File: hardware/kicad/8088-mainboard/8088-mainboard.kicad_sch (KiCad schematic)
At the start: 0 parts

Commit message: Add PSB board design
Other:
- sheet EXPANSION_CONNECTOR ports: added none; removed IO_EXP2_CS, MEM_EXP2_CS
- sheet IO_DECODER ports: added none; removed IO_EXP2_CS
- sheet MEM_DECODER ports: added none; removed MEM_EXP2_CS
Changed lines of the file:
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@@
 	(wire
 		(pts
-			(xy 215.265 77.47) (xy 215.265 43.18)
-		)
-		(stroke
-			(width 0)
-			(type default)
-		)
-	)
-	(wire
-		(pts
 			(xy 108.585 96.52) (xy 113.665 96.52)
 		)
@@
 	(wire
 		(pts
-			(xy 160.655 43.18) (xy 215.265 43.18)
-		)
-		(stroke
-			(width 0)
-			(type default)
-		)
-	)
-	(wire
-		(pts
 			(xy 79.375 107.95) (xy 73.025 107.95)
 		)
@@
 	(wire
 		(pts
-			(xy 207.645 77.47) (xy 207.645 55.88)
-		)
-		(stroke
-			(width 0)
-			(type default)
-		)
-	)
-	(wire
-		(pts
 			(xy 212.725 50.8) (xy 212.725 77.47)
 		)
@@
 	(wire
 		(pts
-			(xy 207.645 55.88) (xy 126.365 55.88)
-		)
-		(stroke
-			(width 0)
-			(type default)
-		)
-	)
-	(wire
-		(pts
 			(xy 217.805 77.47) (xy 217.805 40.64)
 		)
@@
 			)
 		)
-		(pin "MEM_EXP2_CS" input
-			(at 126.365 55.88 0)
-			(effects
-				(font
-					(size 1.27 1.27)
-				)
-				(justify right)
-			)
-		)
 		(instances
 			(project "8088-mainboard"
@@
 			)
 		)
-		(pin "IO_EXP2_CS" input
-			(at 160.655 43.18 0)
-			(effects
-				(font
-					(size 1.27 1.27)
-				)
-				(justify right)
-			)
-		)
 		(instances
 			(project "8088-mainboard"
@@
 			(effects
 				(font
-					(size 1.27 1.27)
-				)
-				(justify right)
-			)
-		)
-		(pin "IO_EXP2_CS" input
-			(at 215.265 77.47 90)
-			(effects
-				(font
-					(size 1.27 1.27)
-				)
-				(justify right)
-			)
-		)
-		(pin "MEM_EXP2_CS" input
-			(at 207.645 77.47 90)
-			(effects
-				(font

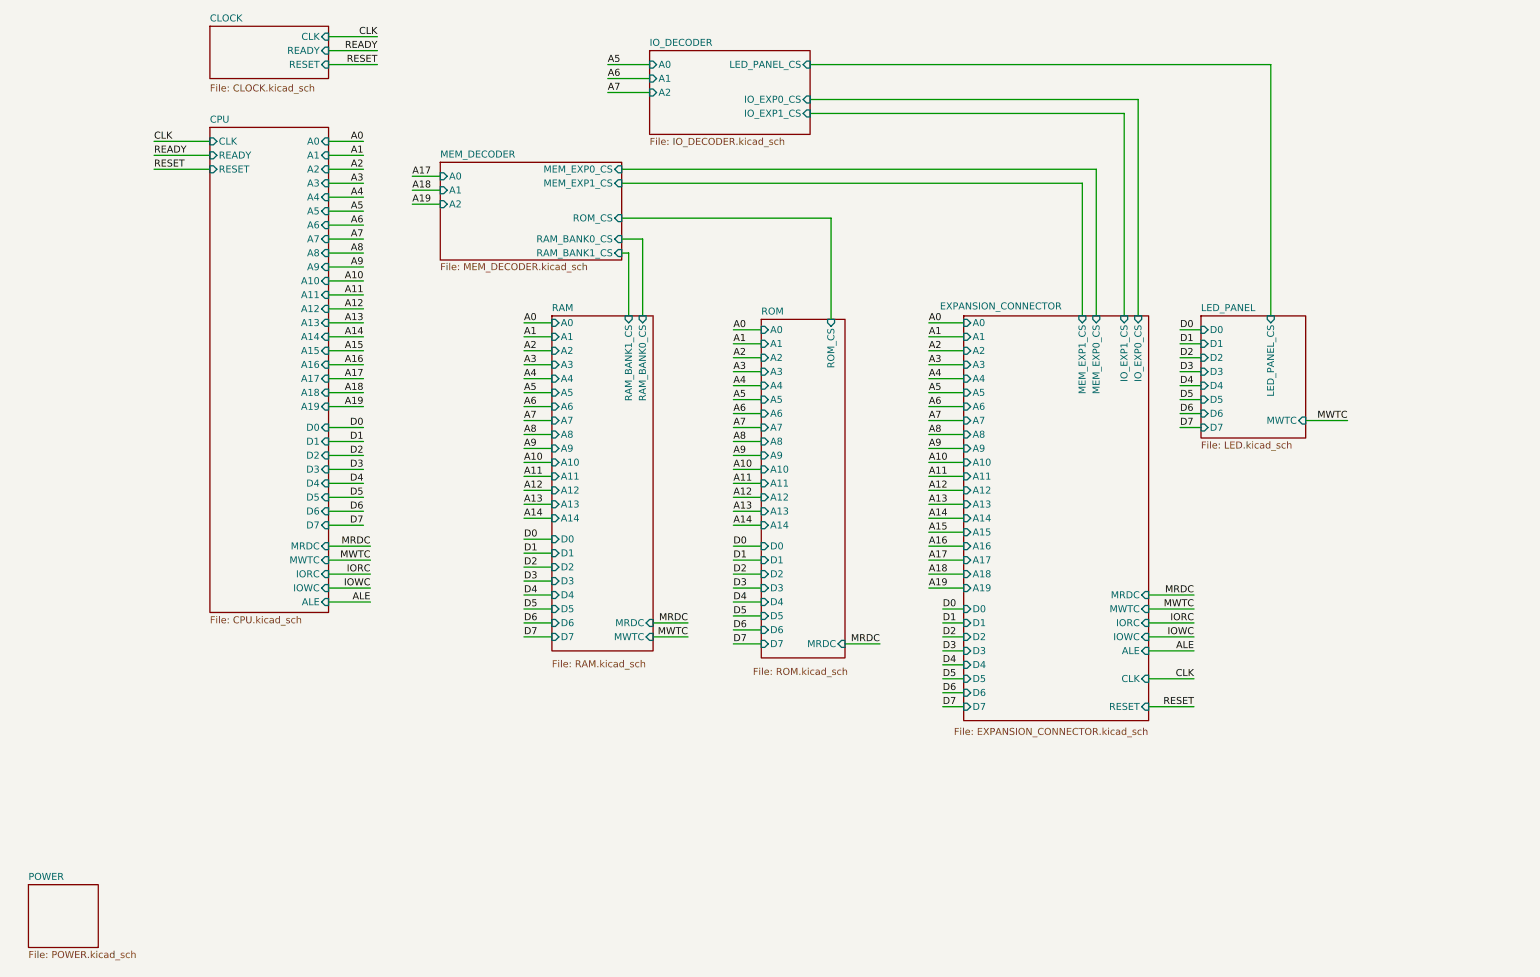
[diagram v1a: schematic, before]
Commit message: Update 8088-mainboard schematics for refined connections and label adjustments
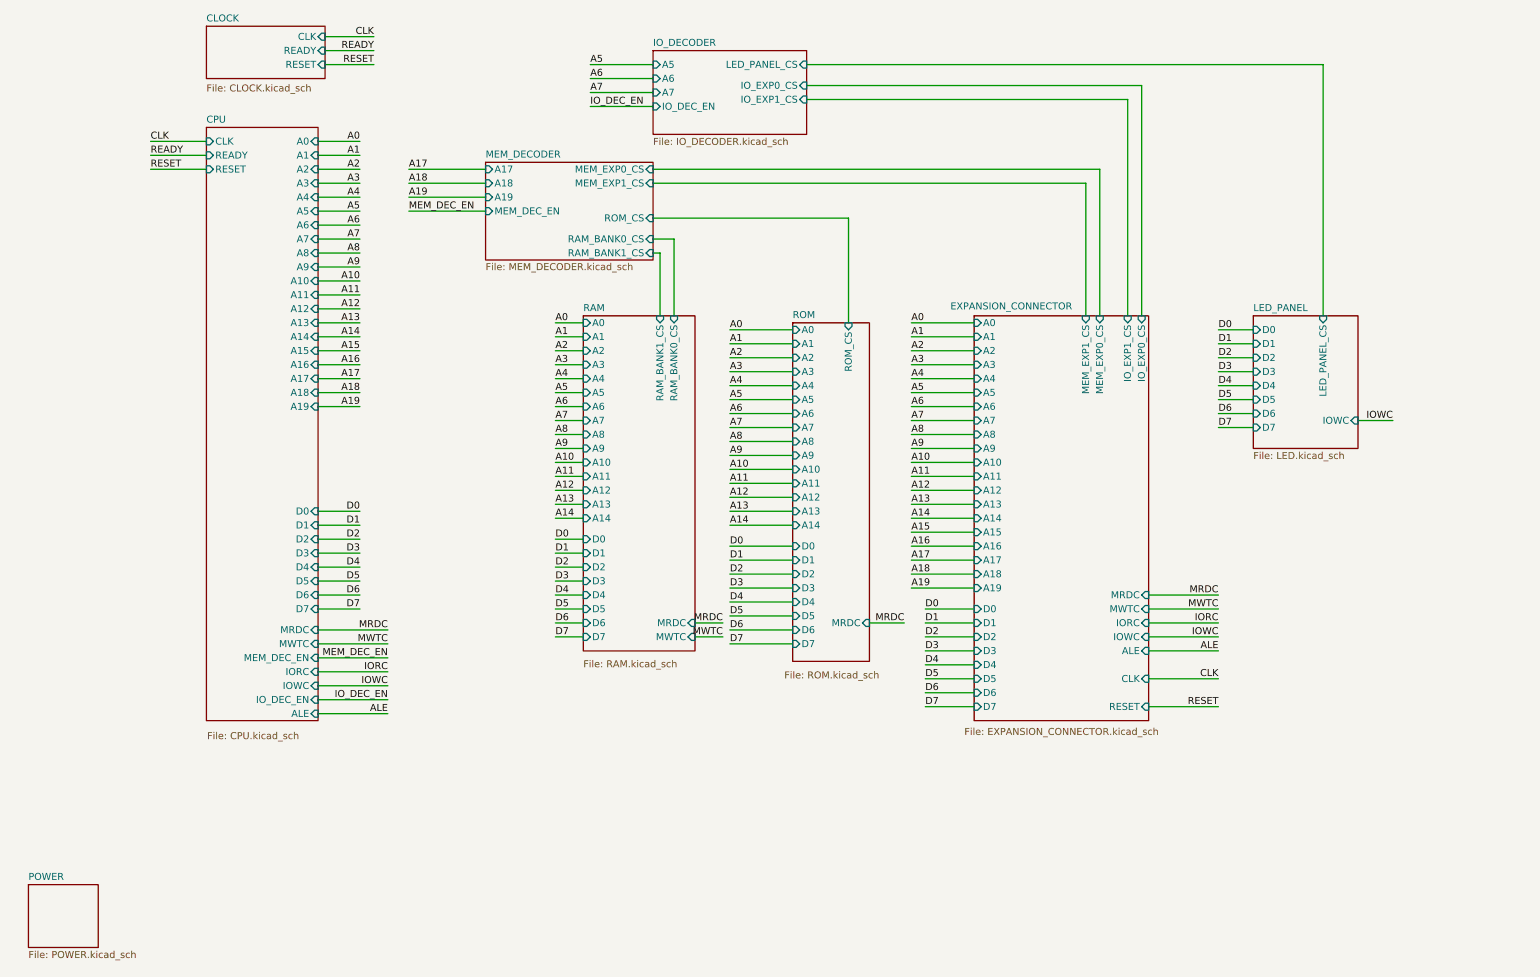
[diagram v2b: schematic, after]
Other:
- sheet CPU ports: added IO_DEC_EN, MEM_DEC_EN; removed none
- sheet IO_DECODER ports: added A5, A6, A7, IO_DEC_EN; removed A0, A1, A2
- sheet LED_PANEL ports: added IOWC; removed MWTC
- sheet MEM_DECODER ports: added A17, A18, A19, MEM_DEC_EN; removed A0, A1, A2

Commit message: Update 8086-mainboard scheme
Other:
- sheet CPU ports: added A[0..19], D[0..7]; removed A0, A1, A10, A11, A12, A13, A14, A15, A16, A17, A18, A19, A2, A3, A4, A5, A6, A7, A8, A9, D0, D1, D2, D3, D4, D5, D6, D7
- sheet EXPANSION_CONNECTOR ports: added A[0..19], D[0..7]; removed A0, A1, A10, A11, A12, A13, A14, A15, A16, A17, A18, A19, A2, A3, A4, A5, A6, A7, A8, A9, D0, D1, D2, D3, D4, D5, D6, D7
- sheet LED_PANEL ports: added D[0..7]; removed D0, D1, D2, D3, D4, D5, D6, D7
- sheet RAM ports: added A[0..19], D[0..7]; removed A0, A1, A10, A11, A12, A13, A14, A2, A3, A4, A5, A6, A7, A8, A9, D0, D1, D2, D3, D4, D5, D6, D7
- sheet ROM ports: added A[0..19], D[0..7]; removed A0, A1, A10, A11, A12, A13, A14, A2, A3, A4, A5, A6, A7, A8, A9, D0, D1, D2, D3, D4, D5, D6, D7

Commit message: Update 8088-mainboard schematics
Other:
- removed sheet LED_PANEL
- sheet CPU ports: added IOM, RD, WR; removed IORC, IOWC, IO_DEC_EN, MEM_DEC_EN, MRDC, MWTC
- sheet EXPANSION_CONNECTOR ports: added IOM, RD, WR; removed IORC, IOWC, MRDC, MWTC
- sheet IO_DECODER ports: added IOM; removed IO_DEC_EN, LED_PANEL_CS
- sheet MEM_DECODER ports: added IOM; removed MEM_DEC_EN
- sheet RAM ports: added RD, WR; removed MRDC, MWTC
- sheet ROM ports: added RD; removed MRDC

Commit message: Finalize 8088 mainboard rev1.0 for production
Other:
- sheet CLOCK ports: added RDY; removed none
- sheet EXPANSION_CONNECTOR ports: added RDY; removed none
- sheet MEM_DECODER ports: added none; removed RAM_BANK1_CS
- sheet RAM ports: added none; removed RAM_BANK1_CS
